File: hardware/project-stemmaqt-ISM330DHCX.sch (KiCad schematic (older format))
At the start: 18 parts, among them J1 SM04B-SRSS-TB(LF)(SN), J2 SM04B-SRSS-TB(LF)(SN), J3 SM04B-SRSS-TB(LF)(SN), U1 TPS7A0218PDBVR, U2 AS7341-DLGT

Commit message: First draft
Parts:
- removed J3: SM04B-SRSS-TB(LF)(SN), JST_SM04B-SRSS-TB(LF)(SN), symbol SM04B-SRSS-TB_LF__SN_:SM04B-SRSS-TB(LF)(SN)
- removed R4: PU, Resistor_SMD:R_0603_1608Metric, symbol Device:R
- removed U1: TPS7A0218PDBVR, SOT95P280X145-5N, symbol TPS7A0233PDBVR:TPS7A0233PDBVR
- removed U2: AS7341-DLGT, PSON80P310X200X110-8N, symbol AS7341-DLGT:AS7341-DLGT
- added J3: Conn_01x04_Male, Connector_PinHeader_2.54mm:PinHeader_1x04_P2.54mm_Vertical, symbol Connector:Conn_01x04_Male
- added U1: ISM330DHCXTR, PQFN50P250X300X86-14N, symbol ISM330DHCXTR:ISM330DHCXTR
- C1: value 1uF -> 10uF
- C2: value 1uF -> 0.1uF; footprint Capacitor_SMD:C_0805_2012Metric -> Capacitor_SMD:C_0603_1608Metric
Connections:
- net +1V8 is gone; now on net VCC: C2.1, C3.1
- net EN is gone; now on net GND: JP1.1 (A)
- net INT is gone; now on net SCL: R1.2
- net GND: now also J3.1 (Pin_1), U1.2 (SDx), U1.3 (SCx), U1.6 (GND), U1.7 (GND-1)
- net SCL: now also U1.13 (SCL); no longer R2.2
- net SDA: now also R2.2, U1.14 (SDA)
- net VCC: now also J3.2 (Pin_2), U1.12 (CS), U1.5 (VDDIO), U1.8 (VDD)
- net SA0: now reaches JP1.2 (C)
- net SA0: now also U1.1 (SDO/SA0)
- new net INT1: J3.3 (Pin_3), U1.4 (INT1)
- new net INT2: J3.4 (Pin_4), U1.9 (INT2)
- no-connect marks 1 -> 2
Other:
- note added: "1: I2C mode"
- note added: "6DoF"
- note added: "Address select"
- note added: "I2C"
- note added: "Power"
- note removed: "Light Sensor"
- note removed: "Regulator"
- note removed: "VEN(HI): ≥1.1V\nVEN(LO): ≤0.3V\nVEN MAX: 6.0V"
- moved on the sheet: C1, D1, H1, H2, H3, H4, JP1, R1, R2, R3

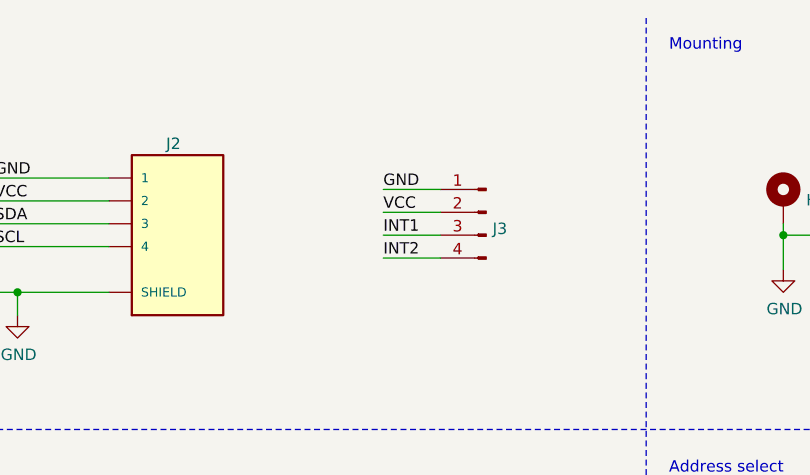
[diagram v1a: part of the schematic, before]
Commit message: Add the battery and interrupt graphics
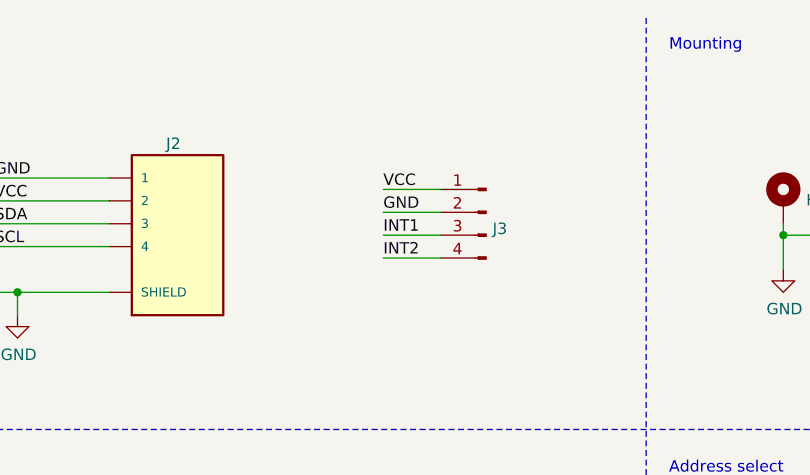
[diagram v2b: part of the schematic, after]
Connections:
- net GND: now also J3.2 (Pin_2); no longer J3.1 (Pin_1)
- net VCC: now also J3.1 (Pin_1); no longer J3.2 (Pin_2)
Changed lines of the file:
@@
 Text Label 7900 1450 0    50   ~ 0
 INT1
+Text Label 7900 1250 0    50   ~ 0
+VCC
 Text Label 7900 1350 0    50   ~ 0
-VCC
-Text Label 7900 1250 0    50   ~ 0
 GND
 Wire Wire Line
@@
 	8150 1450 7900 1450
 Wire Wire Line
+	7900 1250 8150 1250
+Wire Wire Line
 	7900 1350 8150 1350
 Wire Wire Line
-	7900 1250 8150 1250
-Wire Wire Line
 	2300 1450 2300 1500
